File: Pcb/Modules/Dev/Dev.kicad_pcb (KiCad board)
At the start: 2 copper layers, 38.1 x 38.1 mm, 9 parts, among them J1 JACK_STEREO, J2 JACK_RJ45, P1 CONN_02X04, P2 CONN_02X04, Q1 BSS138P, U1 11AA160, X1 HOLE, X2 HOLE

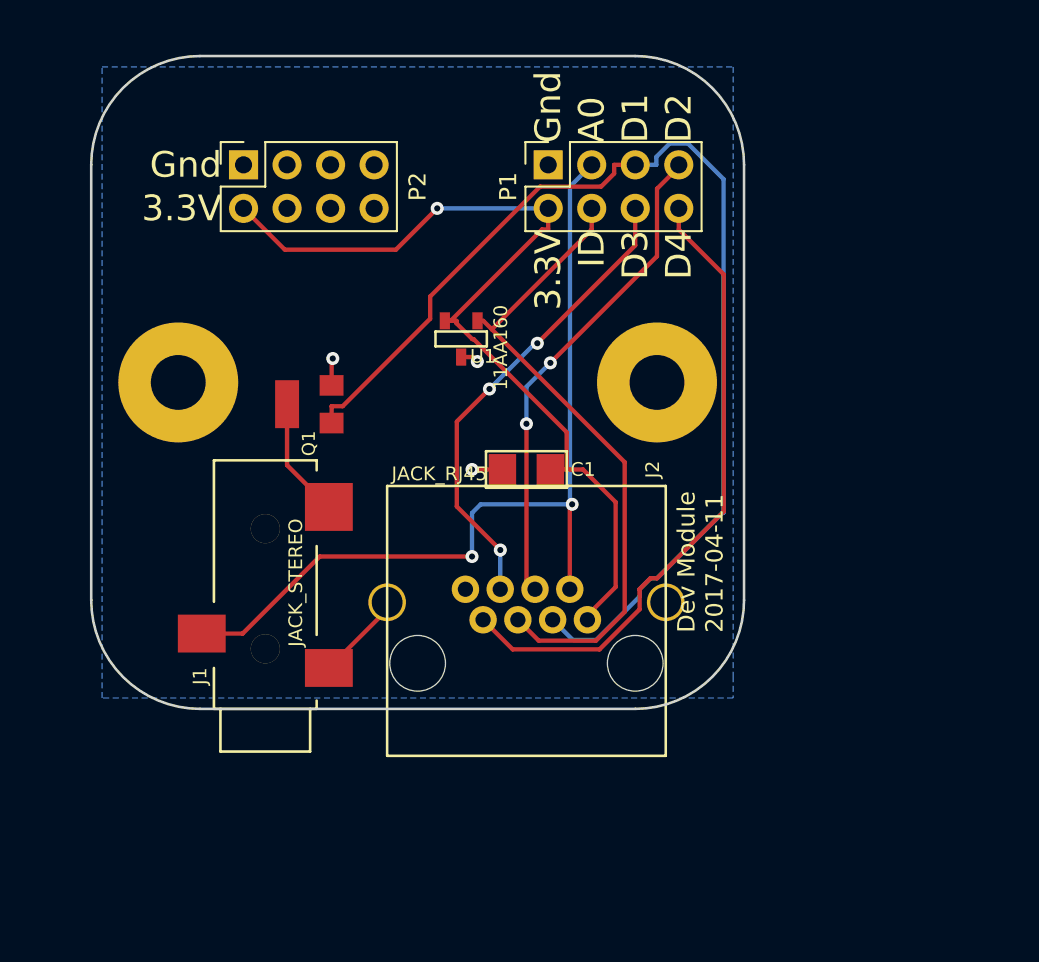
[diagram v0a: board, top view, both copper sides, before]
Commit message: Update module pcbs to common format and fix issues.
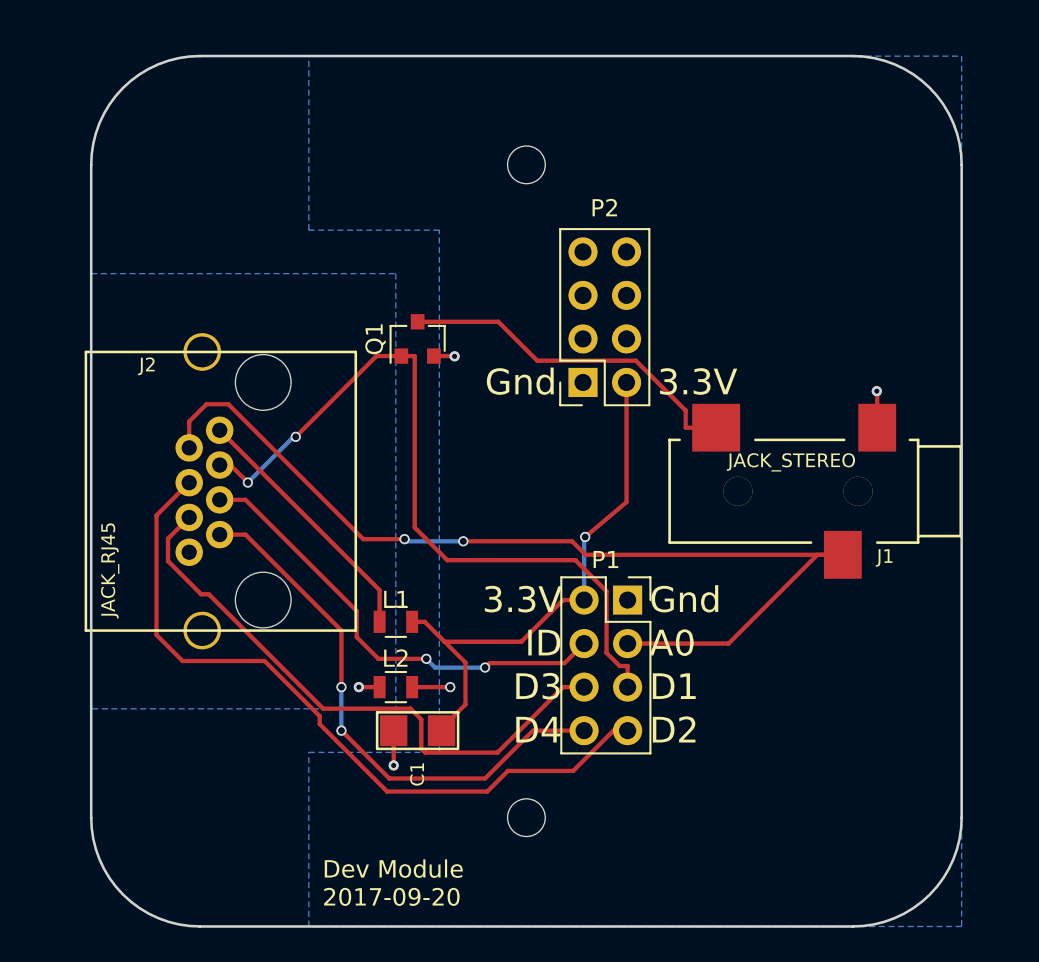
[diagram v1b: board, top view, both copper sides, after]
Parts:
- removed U1: 11AA160, CA6:SOT-23_11AA160
- removed X1, X2: HOLE, CA6:HOLE_3.0mm
- added L1: Ferrite_Bead, Resistors_SMD:R_0805, F.Cu at (43.2, 58.4)
- added L2: Ferrite_Bead, Resistors_SMD:R_0805, F.Cu at (43.2, 62.2)
- added REF**: MountingHole_2.2mm_M2, Mounting_Holes:MountingHole_2.2mm_M2, F.Cu at (50.8, 69.8)
- added REF**1: MountingHole_2.2mm_M2, Mounting_Holes:MountingHole_2.2mm_M2, F.Cu at (50.8, 31.8)
- Q1: value BSS138P -> Q_NMOS_GSD; footprint CA6:SOT23 -> TO_SOT_Packages_SMD:SOT-23
- moved J1 40.2 mm to (73.7, 50.8), turned to 180 degrees
- moved P1 25.8 mm to (56.7, 57.1), turned to 0 degrees
- moved P2 23.5 mm to (54.1, 44.5), turned to 180 degrees
- moved J2 19.3 mm to (33.0, 50.8), turned to 90 degrees
- moved C1 16.5 mm to (44.5, 64.8)
- moved Q1 8.52 mm to (44.5, 41.9)
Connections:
- J2 pad 1: 3V3 -> Net-(J2-Pad1)
- J2 pad 8: GND -> Net-(J2-Pad8)
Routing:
- net /D1: track 65.7 -> 44.0 mm, vias 0 -> 2
- net 3V3: track 53.1 -> 31.6 mm
- net Net-(J2-Pad1): track 0.00 -> 15.0 mm
- net /D2: track 28.7 -> 42.7 mm, vias 2 -> 0
- net Net-(J1-Pad2): track 7.00 -> 20.6 mm
- net /ID: track 37.7 -> 26.8 mm, vias 0 -> 2
- net /D3: track 27.7 -> 34.6 mm, vias 3 -> 0
- net /A0: track 51.6 -> 58.5 mm
- net /D4: track 37.6 -> 31.7 mm, vias 0 -> 2
- net GND: track 9.72 -> 7.62 mm, vias 3 -> 4
- net Net-(J2-Pad8): track 0.00 -> 1.21 mm, vias 0 -> 1
- added copper zone on B.Cu, net Net-(J2-Pad8)
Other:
- board size 38.1 x 38.1 mm -> 50.8 x 50.8 mm
- net class Default: clearance 0.254 -> 0.2; trace_width 0.254 -> 0.25; via_dia 0.762 -> 0.6; via_drill 0.3556 -> 0.4
- rule trace_clearance: 0.254 -> 0.2
- rule trace_min: 0.254 -> 0.2
- rule via_min_drill: 0.3556 -> 0.3
- rule via_min_size: 0.762 -> 0.4
- board text added: "Dev Module 2017-09-20"
- board text removed: "Dev Module 2017-04-11"

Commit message: Add vibration module and fix reversed rj45 plug on dev sensor.
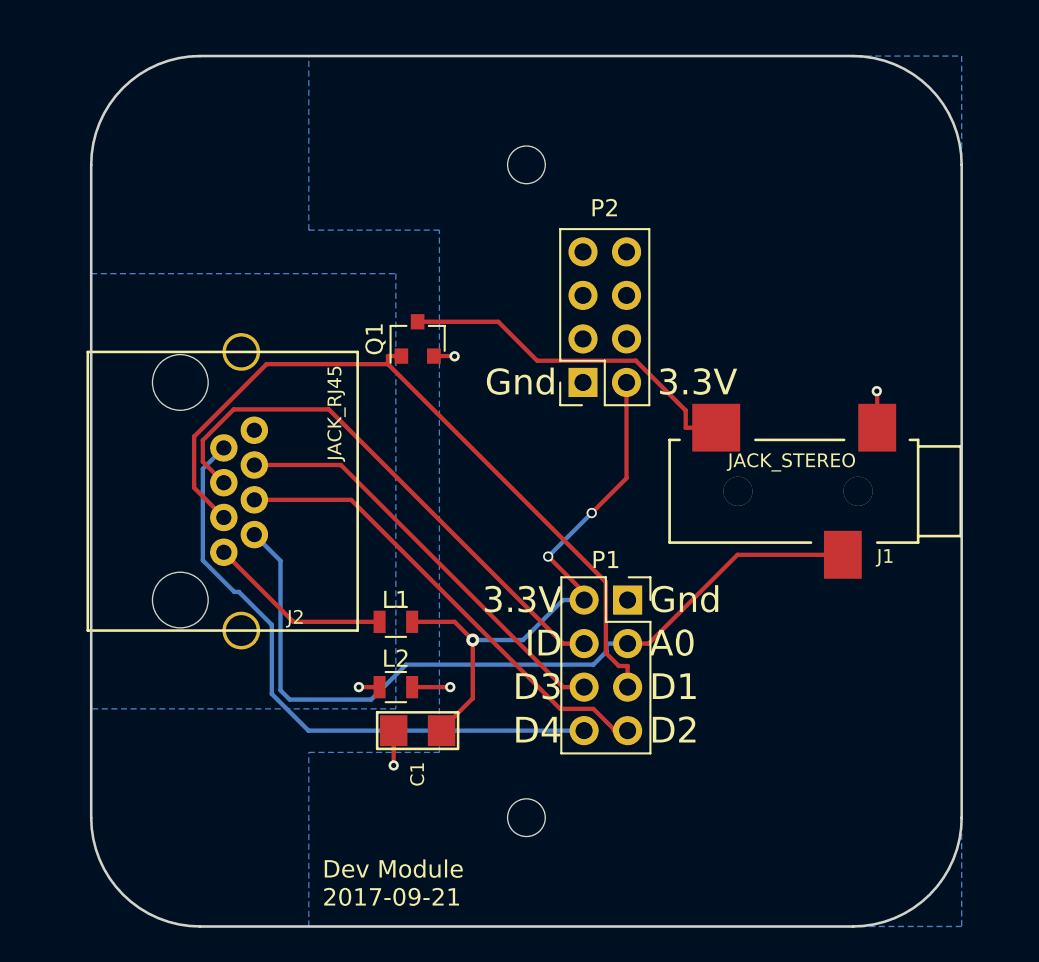
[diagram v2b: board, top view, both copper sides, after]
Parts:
- turned J2 to 270 degrees
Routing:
- net /D2: track 42.7 -> 27.5 mm
- net /A0: track 58.5 -> 46.5 mm, vias 2 -> 0
- net /D3: track 34.6 -> 24.6 mm
- net /ID: track 26.8 -> 31.6 mm, vias 2 -> 0
- net Net-(J2-Pad1): track 15.0 -> 10.8 mm
- net /D4: track 31.7 -> 35.8 mm, vias 2 -> 0
- net 3V3: track 31.6 -> 33.0 mm, vias 1 -> 3
- net /D1: track 44.0 -> 44.7 mm, vias 2 -> 0
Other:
- board text added: "Dev Module 2017-09-21"
- board text removed: "Dev Module 2017-09-20"

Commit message: Update dev module pcb
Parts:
- removed L1, L2: Ferrite_Bead, Resistors_SMD:R_0805
- removed P2: CONN_02X04, Socket_Strips:Socket_Strip_Straight_2x04_Pitch2.54mm
- removed REF**, REF**1: MountingHole_2.2mm_M2, Mounting_Holes:MountingHole_2.2mm_M2
- added SW0: SW_TACTILE, CA6:PTS645, F.Cu at (57.4, 41.9)
- moved P1 22.0 mm to (48.3, 36.8), turned to 180 degrees
- moved C1 21.1 mm to (44.2, 43.7), turned to 180 degrees
- moved J1 15.4 mm to (75.9, 35.6)
- moved J2 15.3 mm to (31.8, 35.6)
- moved Q1 5.93 mm to (50.3, 42.9), turned to 0 degrees
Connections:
- net /A0 renamed /M_0
- net /D1 renamed /M_1
- net /D2 renamed /M_2
- net /D3 renamed /M_4
- net /D4 renamed /M_5
- net /ID renamed /M_3
- J2 pad 1: Net-(J2-Pad1) -> 3V3
- J2 pad 8: Net-(J2-Pad8) -> GND
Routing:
- net /M_2: track 27.5 -> 47.9 mm, vias 0 -> 1
- net /M_5: track 35.8 -> 22.4 mm
- net Net-(J2-Pad1): track 10.8 -> 0.00 mm
- net 3V3: track 33.0 -> 25.6 mm, vias 3 -> 0
- net /M_4: track 24.6 -> 18.1 mm, vias 0 -> 2
- net /M_0: track 46.5 -> 41.5 mm
- net /M_3: track 31.6 -> 35.0 mm
- net /M_1: track 44.7 -> 41.6 mm, vias 0 -> 3
- net Net-(J1-Pad2): track 20.6 -> 18.1 mm, vias 0 -> 2
- net GND: track 7.62 -> 8.89 mm
- net Net-(J2-Pad8): track 1.21 -> 0.00 mm, vias 1 -> 0
- removed copper zone on B.Cu, net Net-(J2-Pad8)
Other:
- board size 50.8 x 50.8 mm -> 50.8 x 20.3 mm
- net class Default: clearance 0.2 -> 0.2032; trace_width 0.25 -> 0.254; via_dia 0.6 -> 0.6604; via_drill 0.4 -> 0.3556
- rule trace_clearance: 0.2 -> 0.2032
- board text added: "Dev Module 2017-10-11"
- board text added: "M_0"
- board text added: "M_1"
- board text added: "M_2"
- board text added: "M_3"
- board text added: "M_4"
- board text added: "M_5"
- board text removed: "A0"
- board text removed: "D1"
- board text removed: "D2"
- board text removed: "D3"
- board text removed: "D4"
- board text removed: "Dev Module 2017-09-21"
- board text removed: "ID"

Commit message: Update dev pcb layout
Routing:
- net GND: track 8.89 -> 91.8 mm, vias 4 -> 5
- net /M_2: track 47.9 -> 98.5 mm, vias 1 -> 3
- net /M_0: track 41.5 -> 59.6 mm, vias 0 -> 1
- net /M_4: track 18.1 -> 31.2 mm, vias 2 -> 0
- net Net-(J1-Pad2): track 18.1 -> 29.6 mm
- net /M_3: track 35.0 -> 46.0 mm
- net 3V3: track 25.6 -> 31.9 mm, vias 0 -> 1
- net /M_5: track 22.4 -> 25.3 mm
- net /M_1: track 41.6 -> 40.5 mm, vias 3 -> 4
- added copper zone on F.Cu, net GND
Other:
- net class Default: trace_width 0.254 -> 1

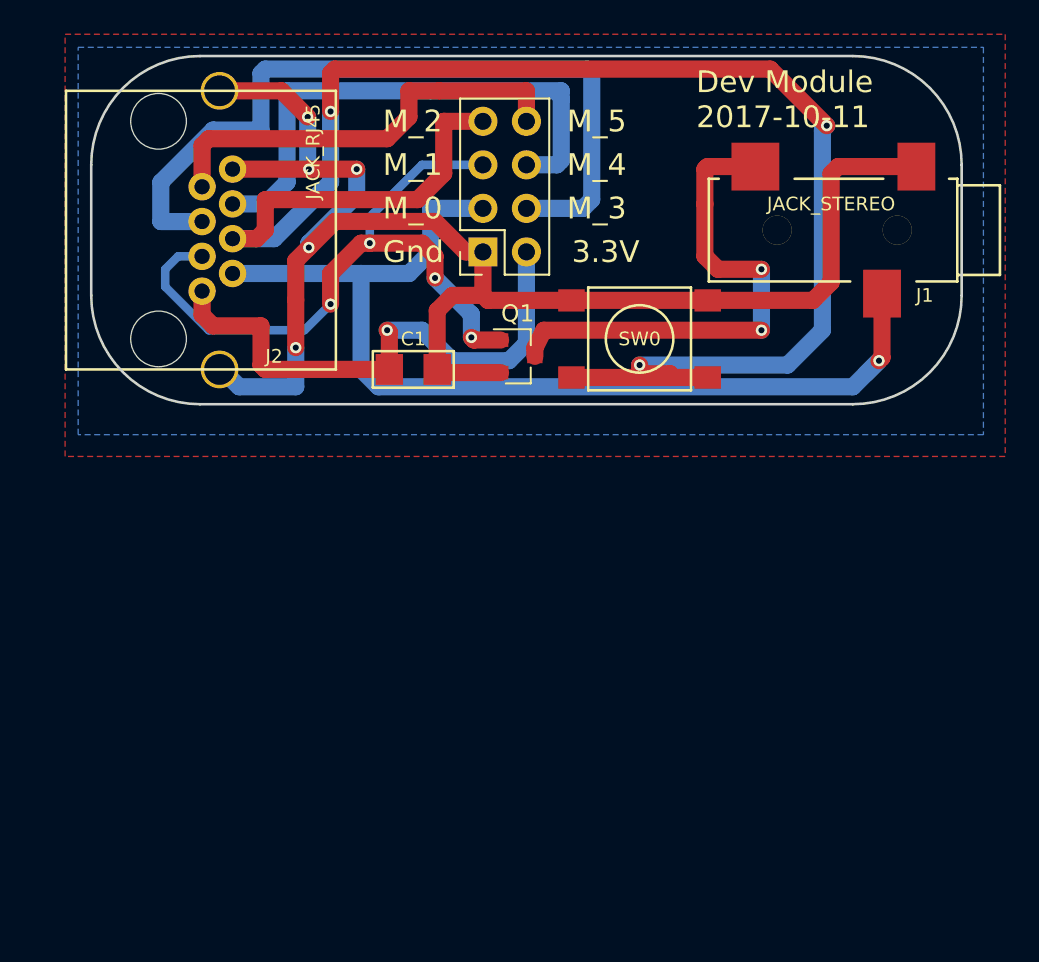
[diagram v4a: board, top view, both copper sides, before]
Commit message: Fix up PCB traces
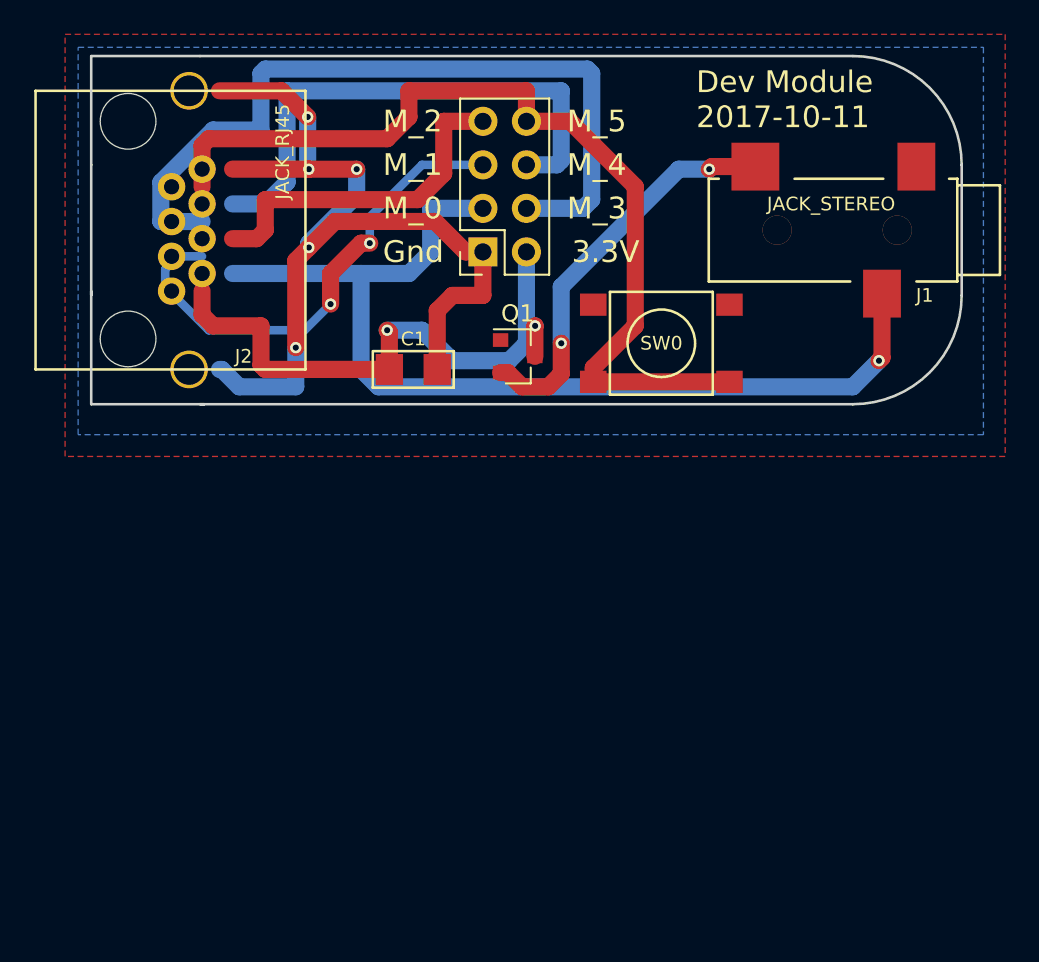
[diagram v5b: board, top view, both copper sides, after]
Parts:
- moved J2 1.78 mm to (30.0, 35.6)
- moved SW0 1.30 mm to (58.7, 42.2)
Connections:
- Q1 pad 1: /M_1 -> (no net)
- Q1 pad 2: GND -> Net-(J1-Pad2)
- Q1 pad 3: Net-(J1-Pad2) -> 3V3
- SW0 pad 3: /M_2 -> /M_5
- SW0 pad 4: /M_2 -> /M_5
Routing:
- net /M_2: track 98.5 -> 20.3 mm, vias 3 -> 0
- net GND: track 91.8 -> 55.9 mm
- net /M_5: track 25.3 -> 60.2 mm
- net /M_1: track 40.5 -> 6.02 mm, vias 4 -> 0
- net 3V3: track 31.9 -> 57.2 mm, vias 1 -> 4
- net /M_3: track 46.0 -> 39.4 mm
- net Net-(J1-Pad2): track 29.6 -> 23.5 mm
- net /M_0: track 59.6 -> 58.5 mm
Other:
- outline, holes or cut-outs redrawn

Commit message: Update pcb layout for modules
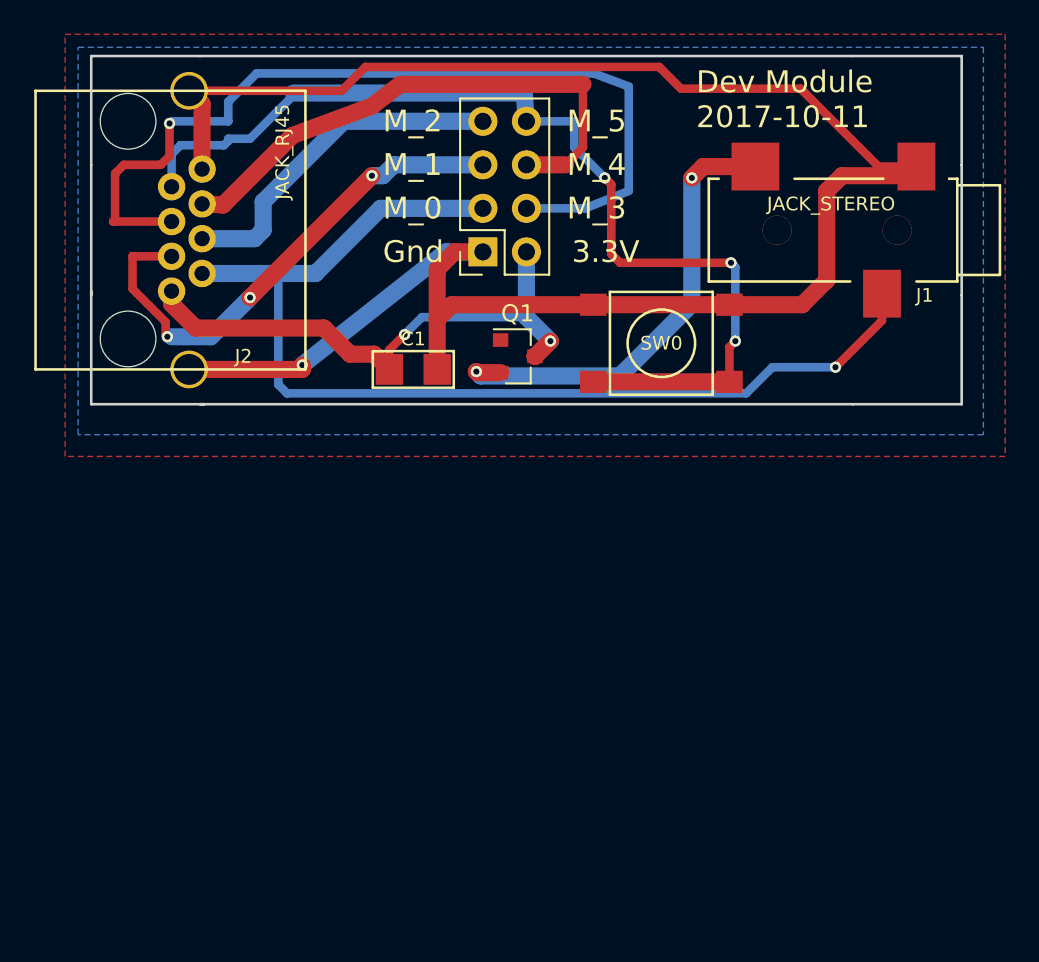
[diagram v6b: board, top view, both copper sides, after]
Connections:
- Q1 pad 1: (no net) -> Net-(Q1-Pad1)
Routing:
- net GND: track 55.9 -> 113.7 mm, vias 5 -> 1
- net 3V3: track 57.2 -> 32.0 mm, vias 4 -> 2
- net /M_1: track 6.02 -> 30.4 mm, vias 0 -> 3
- net /M_3: track 39.4 -> 52.8 mm, vias 0 -> 1
- net /M_0: track 58.5 -> 63.2 mm
- net Net-(J1-Pad2): track 23.5 -> 27.2 mm
- net /M_4: track 31.2 -> 32.1 mm
- net /M_5: track 60.2 -> 59.5 mm, vias 0 -> 3
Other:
- outline, holes or cut-outs redrawn
- net class Default: trace_width 1 -> 0.5
